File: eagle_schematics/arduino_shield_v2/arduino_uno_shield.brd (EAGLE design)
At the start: 53 x 57.1 mm, 20 parts

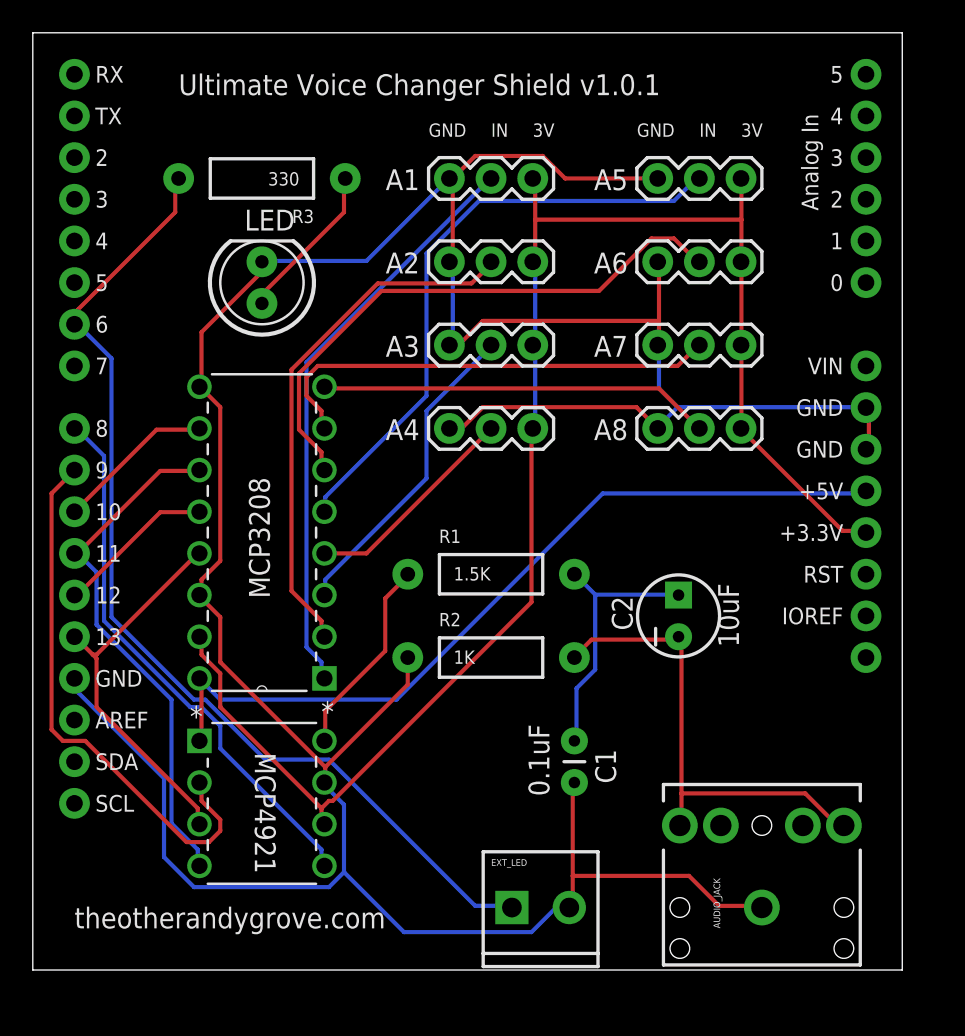
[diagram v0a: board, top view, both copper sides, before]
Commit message: add amplifier
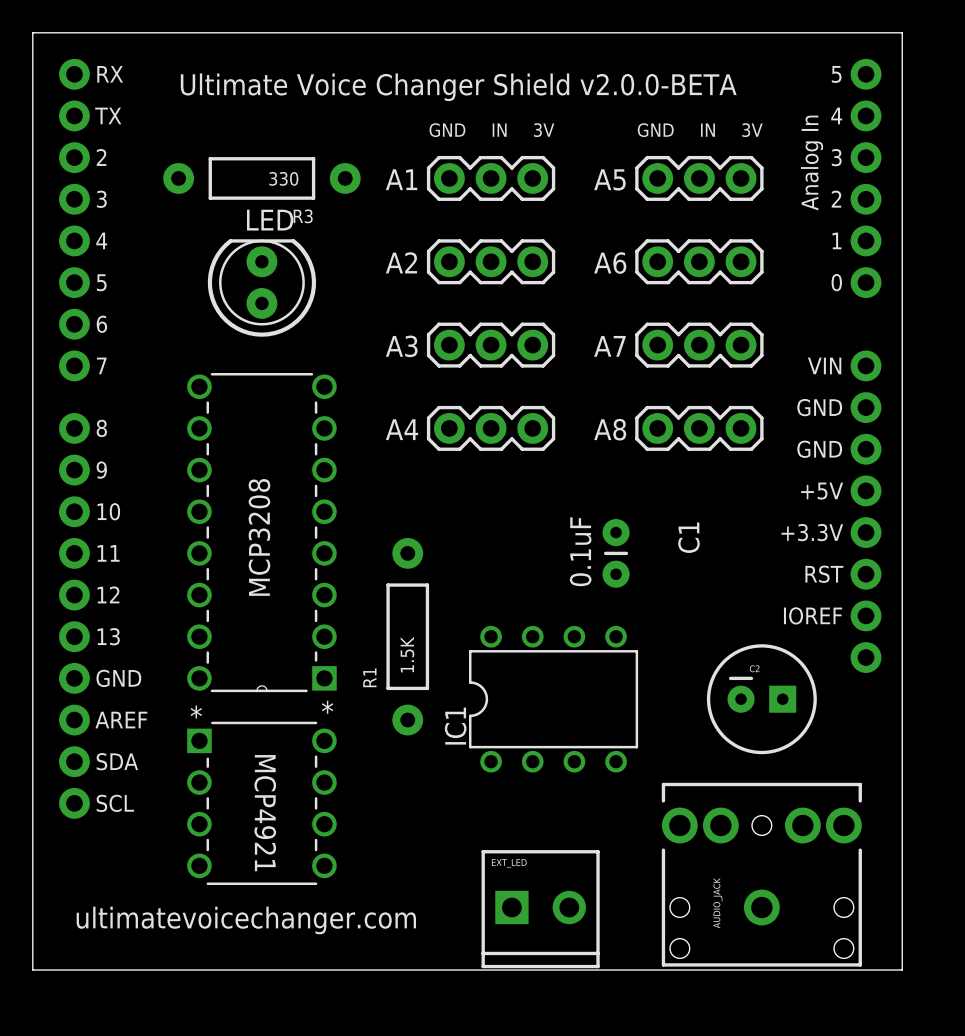
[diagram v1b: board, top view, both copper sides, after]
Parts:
- removed R2: 1K, SparkFun-Passives:AXIAL-0.4
- added IC1: TL072P, linear:DIL08
- C2: value 10uF -> 100uF; device SparkFun-Passives:CPOL-RADIAL-10UF-25V -> SparkFun-Capacitors:CPOL-RADIAL-100UF-25V
- moved C1 13.0 mm to (35.6, 47.0)
- moved C2 7.18 mm to (44.5, 36.8), turned to 0 degrees
- moved R1 6.35 mm to (22.9, 40.6), turned to 90 degrees
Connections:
- removed net N$8: C1.1, C2.1, R1.P$2
- removed net N$9: AUDIO_JACK.RING, AUDIO_JACK.TIP, C2.2, R2.P$2
- new net AUDIO: C1.1, IC1.3, IC1.5, R1.P$2
- new net N$4: C2.1, IC1.1, IC1.2, IC1.6, IC1.7
- new net N$5: AUDIO_JACK.TIP, C2.2
- net 5V: now also IC1.8
- net GND: now also IC1.4; no longer R2.P$1
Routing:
- net GND: track 204.1 -> 0.00 mm
- net 3.3V: track 97.2 -> 0.00 mm
- net N$12: track 62.3 -> 0.00 mm
- net 5V: track 50.5 -> 0.00 mm
- net N$1: track 36.8 -> 0.00 mm
- net AUD: track 35.7 -> 0.00 mm
- net N$16: track 34.9 -> 0.00 mm
- net N$11: track 33.5 -> 0.00 mm
- net CS_DAC: track 33.3 -> 0.00 mm
- net N$2: track 32.1 -> 0.00 mm
- net SPI_MOSI: track 32.0 -> 0.00 mm
- net N$9: track 29.3 -> 0.00 mm
- net N$17: track 28.3 -> 0.00 mm
- net N$18: track 23.9 -> 0.00 mm
- net SPI_CLK: track 23.7 -> 0.00 mm
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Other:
- board text added: "Ultimate Voice Changer Shield v2.0.0-BETA"
- board text added: "ultimatevoicechanger.com"
- board text removed: "Ultimate Voice Changer Shield v1.0.1"
- board text removed: "theotherandygrove.com"

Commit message: working on new board layout with trimpots
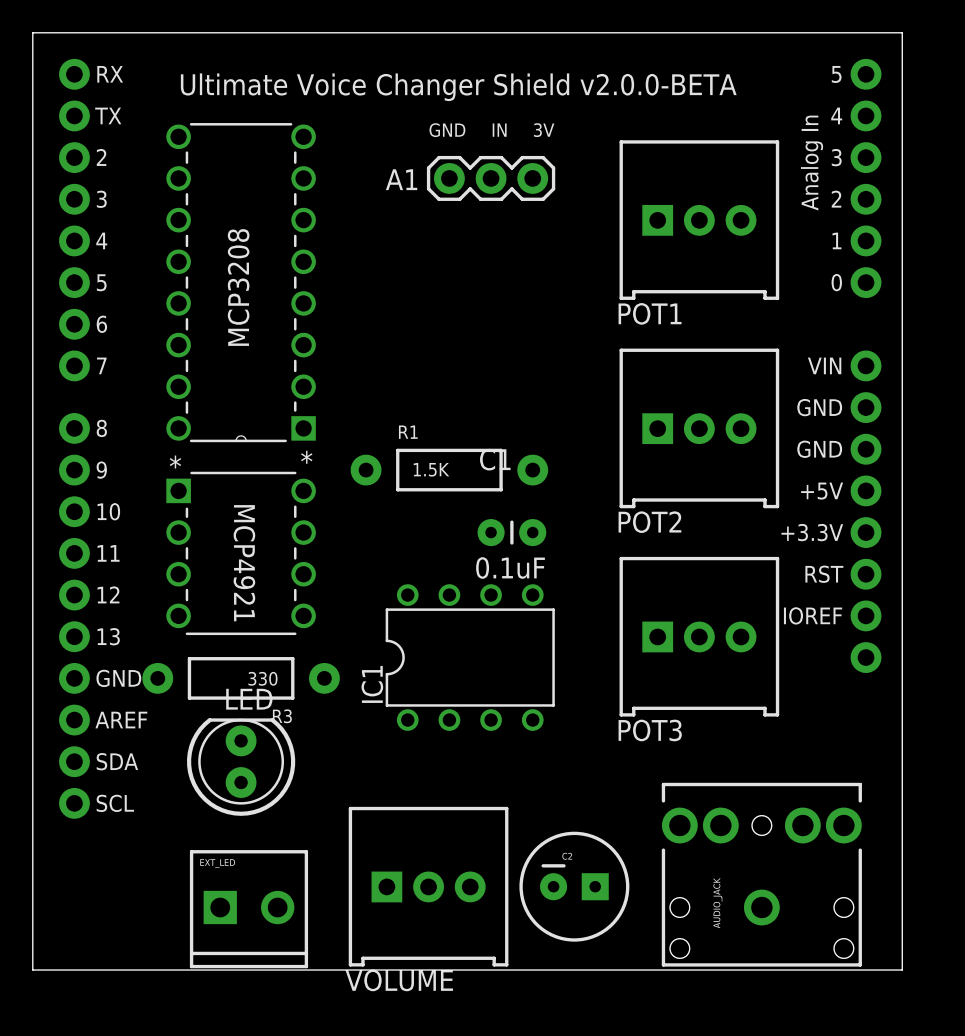
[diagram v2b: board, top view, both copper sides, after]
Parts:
- removed A2, A3, A4, A5, A6, A7, A8: (no value), SparkFun-Connectors:1X03
- added POT1, POT2, POT3, VOLUME: TSR-3386, SparkFun-Electromechanical:3386U
- moved R3 30.5 mm to (12.7, 38.1)
- moved LED 29.2 mm to (12.7, 33.0)
- moved EXT_LED 17.8 mm to (11.4, 24.1)
- moved C2 16.2 mm to (33.0, 25.4)
- moved MCP3208 15.3 mm to (8.89, 71.1)
- moved MCP4921 15.3 mm to (16.5, 41.9)
- moved R1 10.5 mm to (25.4, 50.8), turned to 0 degrees
- moved C1 7.62 mm to (27.9, 47.0), turned to 0 degrees
- moved IC1 5.68 mm to (26.7, 39.4)
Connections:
- removed net N$1: A5.2, MCP3208.5
- removed net N$14: A3.2, MCP3208.3
- removed net N$15: A4.2, MCP3208.4
- removed net N$16: A6.2, MCP3208.6
- removed net N$17: A7.2, MCP3208.7
- removed net N$18: A8.2, MCP3208.8
- removed net N$2: A2.2, MCP3208.2
- new net AUDIO2: IC1.3, IC1.5, VOLUME.2
- new net POT1_INPUT: MCP3208.2, POT1.2
- new net POT2_INPUT: MCP3208.3, POT2.2
- new net POT3_INPUT: MCP3208.4, POT3.2
- net 3.3V: now also POT1.1, POT2.1, POT3.1; no longer A2.3, A3.3, A4.3, A5.3, A6.3, A7.3, A8.3
- net AUDIO: now also VOLUME.1; no longer IC1.3, IC1.5
- net GND: now also MCP3208.5, MCP3208.6, MCP3208.7, MCP3208.8, POT1.3, POT2.3, POT3.3, VOLUME.3; no longer A2.1, A3.1, A4.1, A5.1, A6.1, A7.1, A8.1
- net N$5: now also AUDIO_JACK.RING
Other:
- board text removed: "ultimatevoicechanger.com"

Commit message: change to MCP3204 with 2 trimpot inputs
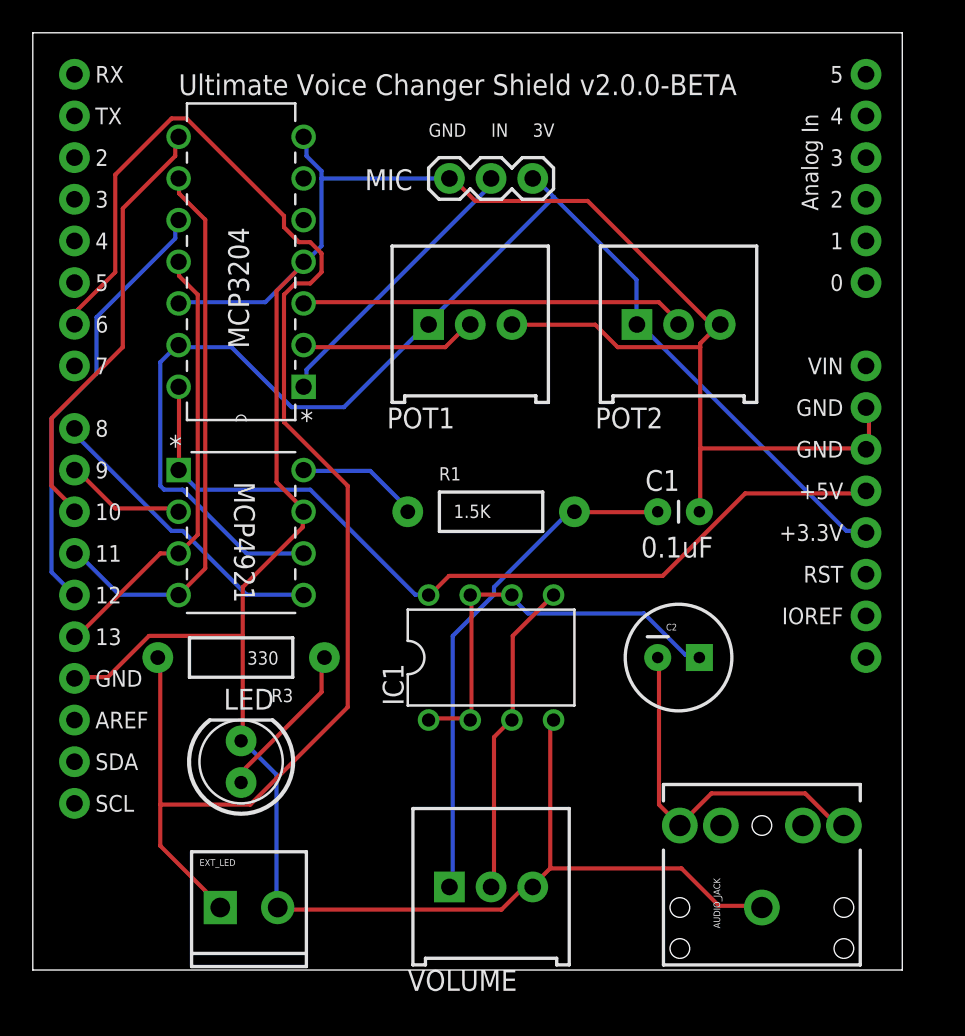
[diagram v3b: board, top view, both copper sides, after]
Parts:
- removed MCP3208: MCP3208-CI/P, Microchip_By_element14_Batch_1:DIP254P762X432-16
- removed POT3: TSR-3386, SparkFun-Electromechanical:3386U
- added MCP3204: MCP3204-CI/P, Microchip_By_element14_Batch_1:DIP254P762X432-14
- moved POT1 15.3 mm to (26.7, 59.7)
- moved C2 15.3 mm to (39.4, 39.4)
- moved C1 10.2 mm to (38.1, 48.3)
- moved POT2 6.48 mm to (39.4, 59.7)
- moved VOLUME 3.81 mm to (27.9, 25.4)
- moved R1 3.59 mm to (27.9, 48.3)
- moved MCP4921 1.27 mm to (16.5, 43.2)
- moved IC1 1.27 mm to (27.9, 39.4)
- moved R3 1.27 mm to (12.7, 39.4)
- renumbered A1 to MIC
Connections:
- removed net POT3_INPUT: MCP3208.4, POT3.2
- net 3.3V: now also MCP3204.13; no longer MCP3208.15, POT3.1
- net 5V: now also MCP3204.14; no longer MCP3208.16
- net AUD: now also MCP3204.1; no longer MCP3208.1
- net CS_ADC: now also MCP3204.8; no longer MCP3208.10
- net GND: now also MCP3204.12, MCP3204.4, MCP3204.7; no longer MCP3208.14, MCP3208.5, MCP3208.6, MCP3208.7, MCP3208.8, MCP3208.9, POT3.3
- net POT1_INPUT: now also MCP3204.2; no longer MCP3208.2
- net POT2_INPUT: now also MCP3204.3; no longer MCP3208.3
- net SPI_CLK: now also MCP3204.11; no longer MCP3208.13
- net SPI_MISO: now also MCP3204.10; no longer MCP3208.12
- net SPI_MOSI: now also MCP3204.9; no longer MCP3208.11
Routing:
- net GND: track 0.00 -> 177.9 mm
- net N$12: track 0.00 -> 89.5 mm
- net 3.3V: track 0.00 -> 80.2 mm
- net 5V: track 0.00 -> 52.8 mm
- net SPI_MOSI: track 0.00 -> 34.2 mm
- net AUDIO: track 0.00 -> 31.5 mm
- net SPI_CLK: track 0.00 -> 27.2 mm
- net CS_ADC: track 0.00 -> 26.7 mm
- net SPI_MISO: track 0.00 -> 26.6 mm
- net N$4: track 0.00 -> 25.9 mm
- net POT2_INPUT: track 0.00 -> 23.5 mm
- net N$5: track 0.00 -> 22.5 mm
- net AUDIO2: track 0.00 -> 19.4 mm
- net N$11: track 0.00 -> 18.4 mm
- net AUD: track 0.00 -> 17.5 mm
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
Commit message: refine board layout
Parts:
- removed FRAME3: FRAME-LETTER, SparkFun-Aesthetics:CREATIVE_COMMONS
- moved POT1 15.3 mm to (40.6, 66.0)
- moved POT2 7.73 mm to (40.6, 52.1)
- moved C1 6.84 mm to (31.8, 50.8), turned to 270 degrees
- moved R1 4.58 mm to (24.1, 50.8)
- moved C2 1.80 mm to (40.6, 38.1)
- moved IC1 1.27 mm to (27.9, 40.6)
- moved MIC 1.27 mm to (24.1, 68.6)
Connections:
- removed net AUD: MCP3204.1, MIC.2
- new net MIC: MCP3204.1, MIC.3
- net 3.3V: now also MIC.1; no longer MIC.3
- net GND: now also MIC.2; no longer MIC.1
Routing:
- net N$12: track 89.5 -> 67.7 mm
- net MIC: track 0.00 -> 18.1 mm
- net AUD: track 17.5 -> 0.00 mm
- net POT1_INPUT: track 10.8 -> 27.3 mm
- net POT2_INPUT: track 23.5 -> 31.2 mm
- net GND: track 177.9 -> 172.7 mm
- net N$3: track 7.51 -> 2.56 mm
- net SPI_MOSI: track 34.2 -> 38.1 mm
- net 3.3V: track 80.2 -> 82.9 mm
- net N$4: track 25.9 -> 28.4 mm
- net N$5: track 22.5 -> 20.0 mm
- net AUDIO: track 31.5 -> 29.6 mm
- net AUDIO2: track 19.4 -> 20.7 mm
- net 5V: track 52.8 -> 51.8 mm
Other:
- board text added: "Ultimate Voice Changer v2.0.0"
- board text removed: "Ultimate Voice Changer Shield v2.0.0-BETA"

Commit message: Save
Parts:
- IC1: value TL072P -> TLV2462CP
- renumbered R3 to R2
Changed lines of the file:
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@@
 <?xml version="1.0" encoding="utf-8"?>
 <!DOCTYPE eagle SYSTEM "eagle.dtd">
-<eagle version="7.5.0">
+<eagle version="7.1.0">
 <drawing>
 <settings>
@@
 <wire x1="53.01" y1="77.46" x2="0" y2="77.46" width="0" layer="20"/>
 <wire x1="0" y1="77.46" x2="0" y2="20.32" width="0" layer="20"/>
-<text x="26.67" y="71.12" size="0.8128" layer="21">GND</text>
-<text x="30.48" y="71.12" size="0.8128" layer="21">IN</text>
-<text x="24.13" y="71.12" size="0.8128" layer="21">3V</text>
-<text x="13.97" y="73.66" size="1.27" layer="21">Ultimate Voice Changer v2.0.0</text>
+<text x="25.4" y="71.12" size="0.8128" layer="21" font="vector" ratio="15">GND</text>
+<text x="29.21" y="71.12" size="0.8128" layer="21" font="vector" ratio="15">IN</text>
+<text x="22.86" y="71.12" size="0.8128" layer="21" font="vector" ratio="15">3V</text>
+<text x="13.97" y="73.66" size="1.27" layer="21" font="vector" ratio="20">Ultimate Voice Changer v2.0.0</text>
 </plain>
 <attributes>
@@
 </autorouter>
 <elements>
-<element name="AUDIO_JACK" library="SparkFun-Connectors" package="AUDIO-JACK" value="" x="44.45" y="24.13" rot="R90"/>
+<element name="AUDIO_JACK" library="SparkFun-Connectors" package="AUDIO-JACK" value="" x="44.45" y="24.13" smashed="yes" rot="R90">
+<attribute name="NAME" x="50.8" y="33.02" size="0.8128" layer="25" font="vector" ratio="15" rot="R180"/>
+<attribute name="VALUE" x="43.18" y="22.86" size="0.4064" layer="27" rot="R90"/>
+</element>
 <element name="C1" library="SparkFun-Passives" package="CAP-PTH-SMALL" value="0.1uF" x="31.75" y="50.8" smashed="yes" rot="R270">
-<attribute name="NAME" x="33.02" y="51.562" size="1.27" layer="25" rot="R270"/>
-<attribute name="VALUE" x="28.956" y="51.816" size="1.27" layer="21" rot="R270"/>
+<attribute name="NAME" x="33.02" y="49.022" size="0.8128" layer="25" rot="R270"/>
+<attribute name="VALUE" x="32.766" y="53.086" size="0.8128" layer="21" rot="R270"/>
 </element>
 <element name="LED" library="SparkFun-LED" package="LED5MM" value="" x="12.7" y="33.02" smashed="yes" rot="R90">
-<attribute name="NAME" x="14.7066" y="37.465" size="1.27" layer="25" ratio="10" rot="R180"/>
+<attribute name="NAME" x="10.8966" y="36.195" size="0.8128" layer="25" font="vector" ratio="15" rot="R180"/>
 <attribute name="VALUE" x="14.5034" y="36.2204" size="1.27" layer="27" ratio="10" rot="R90"/>
 </element>
@@
 <attribute name="SUPPLIER" value="Microchip" x="8.89" y="71.12" size="1.778" layer="27" rot="R180" display="off"/>
 <attribute name="OC_FARNELL" value="9758593" x="8.89" y="71.12" size="1.778" layer="27" rot="R180" display="off"/>
-<attribute name="NAME" x="13.1826" y="58.2168" size="1.27" layer="25" ratio="10" rot="SR90"/>
+<attribute name="NAME" x="13.1826" y="60.7568" size="0.8128" layer="25" font="vector" ratio="15" rot="SR90"/>
 </element>
 <element name="MCP4921" library="Microchip_By_element14_Batch_1" package="DIP254P762X432-8" value="MCP4921-E/P" x="16.51" y="43.18" smashed="yes">
@@
 <attribute name="SUPPLIER" value="Microchip" x="16.51" y="43.18" size="1.778" layer="27" display="off"/>
 <attribute name="OC_FARNELL" value="1332112" x="16.51" y="43.18" size="1.778" layer="27" display="off"/>
-<attribute name="NAME" x="12.2682" y="50.0888" size="1.27" layer="25" ratio="10" rot="SR270"/>
+<attribute name="NAME" x="12.2682" y="50.0888" size="0.8128" layer="25" font="vector" ratio="15" rot="SR270"/>
 </element>
 <element name="MIC" library="SparkFun-Connectors" package="1X03" value="" x="24.13" y="68.58" smashed="yes">
-<attribute name="NAME" x="18.9738" y="67.8688" size="1.27" layer="25" ratio="10"/>
+<attribute name="NAME" x="20.2438" y="69.1388" size="0.8128" layer="25" font="vector" ratio="15"/>
 <attribute name="VALUE" x="22.86" y="65.405" size="1.27" layer="27"/>
 </element>
-<element name="R1" library="SparkFun-Passives" package="AXIAL-0.4" value="1.5K" x="24.13" y="50.8"/>
-<element name="R3" library="SparkFun-Passives" package="AXIAL-0.4" value="330" x="12.7" y="39.37" rot="R180"/>
+<element name="R1" library="SparkFun-Passives" package="AXIAL-0.4" value="1.5K" x="24.13" y="50.8" smashed="yes">
+<attribute name="NAME" x="20.955" y="52.705" size="0.8128" layer="25" font="vector" ratio="15"/>
+<attribute name="VALUE" x="21.844" y="50.419" size="0.8128" layer="21" font="vector" ratio="15"/>
+</element>
+<element name="R2" library="SparkFun-Passives" package="AXIAL-0.4" value="330" x="12.7" y="39.37" rot="R180"/>
 <element name="U$1" library="SparkFun-Boards" package="UNO_R3_SHIELD" value="ARDUINO_R3_SHIELD" x="0" y="20.32"/>
-<element name="EXT_LED" library="SparkFun-Connectors" package="SCREWTERMINAL-3.5MM-2" value="M023.5MM" x="11.43" y="24.13"/>
-<element name="IC1" library="linear" package="DIL08" value="TL072P" x="27.94" y="40.64"/>
-<element name="C2" library="SparkFun-Capacitors" package="CPOL-RADIAL-100UF-25V" value="100uF" x="40.64" y="38.1"/>
-<element name="VOLUME" library="SparkFun-Electromechanical" package="3386U" value="TSR-3386" x="27.94" y="25.4">
+<element name="EXT_LED" library="SparkFun-Connectors" package="SCREWTERMINAL-3.5MM-2" value="M023.5MM" x="11.43" y="24.13" smashed="yes">
+<attribute name="NAME" x="10.16" y="27.94" size="0.8128" layer="25" font="vector" ratio="15"/>
+</element>
+<element name="IC1" library="linear" package="DIL08" value="TLV2462CP" x="27.94" y="40.64" smashed="yes">
+<attribute name="VALUE" x="25.654" y="40.005" size="0.8128" layer="21" font="vector" ratio="15"/>
+</element>
+<element name="C2" library="SparkFun-Capacitors" package="CPOL-RADIAL-100UF-25V" value="100uF" x="40.64" y="38.1" smashed="yes">
+<attribute name="VALUE" x="38.735" y="33.782" size="0.8128" layer="21" font="vector" ratio="15"/>
+<attribute name="NAME" x="39.878" y="39.751" size="0.8128" layer="25" font="vector" ratio="15"/>
+</element>
+<element name="VOLUME" library="SparkFun-Electromechanical" package="3386U" value="TSR-3386" x="27.94" y="25.4" smashed="yes">
 <attribute name="PROD_ID" value="RES-09730" x="27.94" y="25.4" size="1.778" layer="27" display="off"/>
-</element>
-<element name="POT1" library="SparkFun-Electromechanical" package="3386U" value="TSR-3386" x="40.64" y="66.04">
+<attribute name="NAME" x="26.67" y="31.75" size="0.8128" layer="25" font="vector" ratio="15"/>
+</element>
+<element name="POT1" library="SparkFun-Electromechanical" package="3386U" value="TSR-3386" x="40.64" y="66.04" smashed="yes">
 <attribute name="PROD_ID" value="RES-09730" x="40.64" y="66.04" size="1.778" layer="27" display="off"/>
-</element>
-<element name="POT2" library="SparkFun-Electromechanical" package="3386U" value="TSR-3386" x="40.64" y="52.07">
+<attribute name="NAME" x="35.56" y="59.69" size="0.8128" layer="25" font="vector" ratio="15"/>
+</element>
+<element name="POT2" library="SparkFun-Electromechanical" package="3386U" value="TSR-3386" x="40.64" y="52.07" smashed="yes">
 <attribute name="PROD_ID" value="RES-09730" x="40.64" y="52.07" size="1.778" layer="27" display="off"/>
+<attribute name="NAME" x="35.56" y="45.72" size="0.8128" layer="25" font="vector" ratio="15"/>
 </element>
 </elements>
@@
 <signal name="N$10">
 <contactref element="LED" pad="A"/>
-<contactref element="R3" pad="P$1"/>
+<contactref element="R2" pad="P$1"/>
 <wire x1="12.8016" y1="32.4612" x2="12.8016" y2="31.7754" width="0.254" layer="1"/>
 <wire x1="17.6022" y1="37.2618" x2="12.8016" y2="32.4612" width="0.254" layer="1"/>
@@
 <signal name="N$12">
 <contactref element="U$1" pad="D6"/>
-<contactref element="R3" pad="P$2"/>
+<contactref element="R2" pad="P$2"/>
 <contactref element="EXT_LED" pad="1"/>
 <wire x1="7.7724" y1="27.8892" x2="7.7724" y2="39.3192" width="0.254" layer="1"/>
